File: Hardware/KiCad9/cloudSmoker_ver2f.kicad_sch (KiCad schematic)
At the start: 98 parts, among them J1 Conn_01x02_Pin, J10 Conn_01x04_Pin, J11 Conn_01x04_Pin, J12 AudioJack2_SwitchT, J13 AudioJack2_SwitchT, J14 Conn_01x04_Pin, J15 Conn_01x04_Pin, J16 AudioJack2_SwitchT, J2 Conn_01x04_Socket, J3 Conn_01x04_Pin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

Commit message: hardware: update cloudSmoker_ver2f
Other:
- note added: "Note: During actual board assembly, 9.1k ohm resistors were substituted for the nine 10k ohm resistors due to design values being out of stock. Immaterial impacts: 1) RC filter shifts from 16 to 17 Hz 2) Pull-ups slightly stronger"

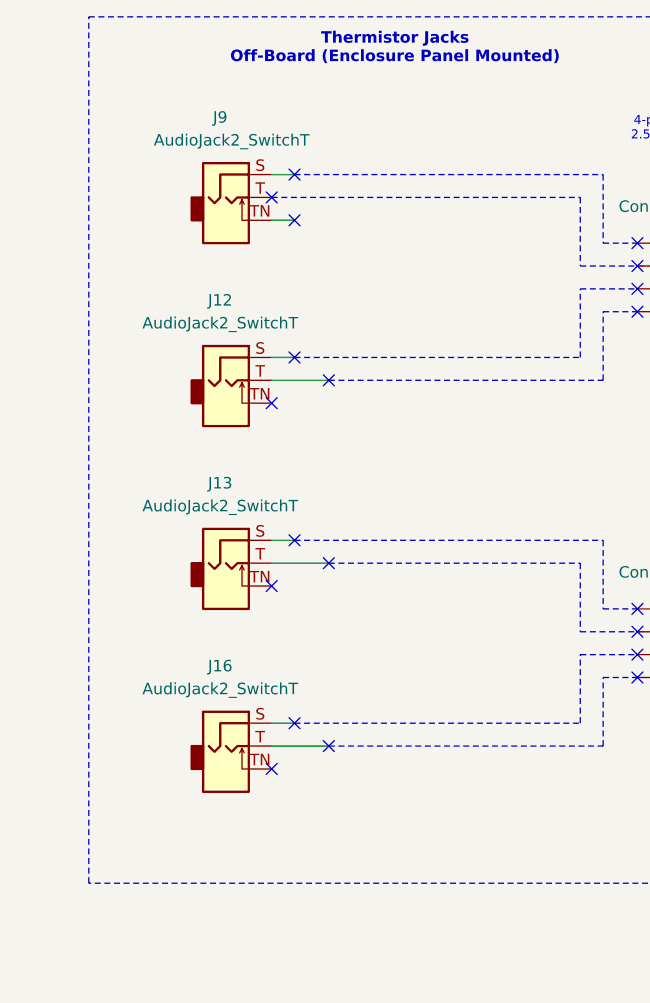
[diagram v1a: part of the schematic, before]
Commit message: update schematic audio jack symbol
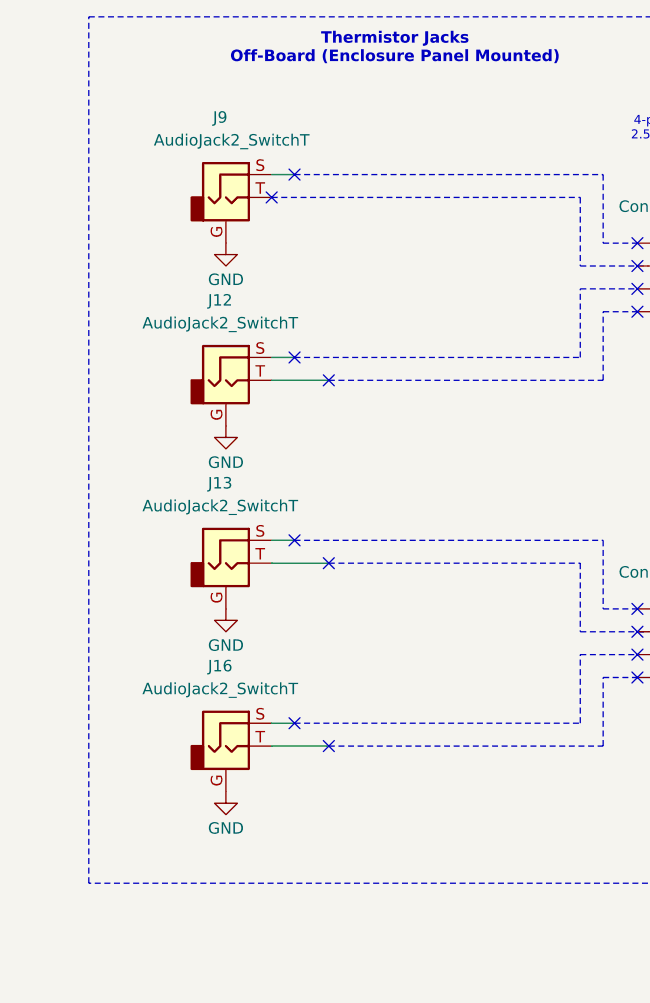
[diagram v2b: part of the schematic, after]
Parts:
- J12, J13, J16, J9: symbol Connector_Audio:AudioJack2_SwitchT -> Connector_Audio:AudioJack2_Ground
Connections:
- net GND: now also J12.G, J13.G, J16.G, J9.G
- no-connect marks 36 -> 32
